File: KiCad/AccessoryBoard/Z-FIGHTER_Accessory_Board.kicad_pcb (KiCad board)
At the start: 2 copper layers, 100 x 75 mm, 24 parts, among them J7 ST7920 Graphic LCD, J9 Conn_02x13_Odd_Even, Q1 BC337, Q2 BC337, SW1 Up (A0), SW2 Down (A1), SW3 Left (A2), SW4 Right (A3), SW5 A (A4), SW6 B (A5)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

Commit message: Updated Accessory Board
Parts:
- J7: footprint Connector_PinSocket_2.54mm:PinSocket_1x20_P2.54mm_Vertical -> Connector_PinSocket_2.54mm:PinSocket_1x20_P2.54mm_Horizontal
- moved J7 6.98 mm to (81.5, 105.6)
- moved Q1 2.44 mm to (81.5, 108.8)
- moved Q2 2.44 mm to (129.8, 108.8)
- moved RB1 2.44 mm to (86.6, 111.3)
- moved RB2 0.44 mm to (138.2, 113.9)
- moved D2 0.10 mm to (145.8, 108.8)
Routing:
- net PB4S: track 80.6 -> 73.6 mm
- net PC0S: track 76.6 -> 69.6 mm
- net PB7S: track 80.6 -> 73.6 mm
- net PB6S: track 80.6 -> 73.6 mm
- net PB5S: track 80.6 -> 73.6 mm
- net PB0S: track 99.2 -> 92.2 mm
- net PB3S: track 77.0 -> 70.0 mm
- net PC2S: track 82.0 -> 75.0 mm
- net PB2S: track 85.2 -> 78.2 mm
- net PC1S: track 79.5 -> 72.6 mm
- net BLK: track 7.72 -> 3.32 mm
- net PB1S: track 87.9 -> 85.0 mm
- net Net-(BZ1-Pad2): track 26.9 -> 25.8 mm
- net Net-(Q2-Pad2): track 10.3 -> 9.50 mm
- net PC3S: track 66.9 -> 66.1 mm
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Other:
- board text added: "Accessory Board Rev. 1c"
- board text removed: "Accessory Board Rev. 1b"

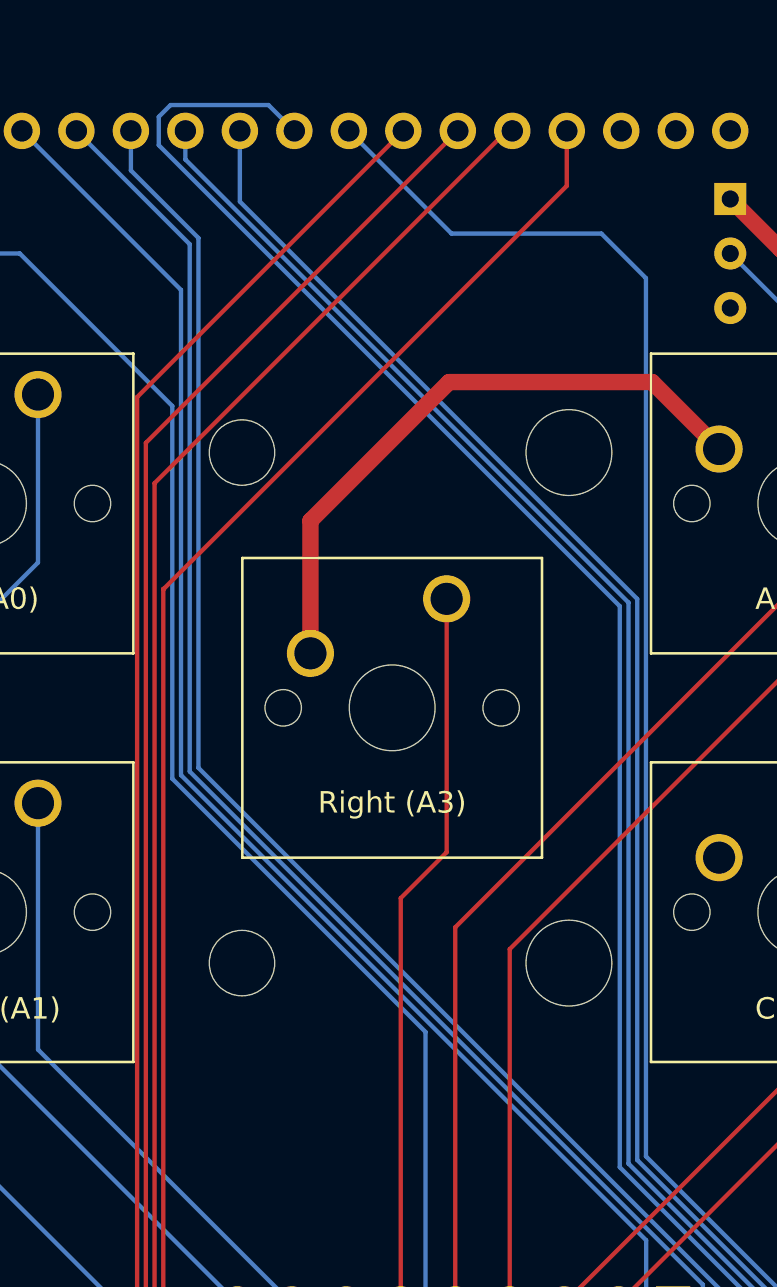
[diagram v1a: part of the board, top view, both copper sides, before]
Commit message: Adjusted routing
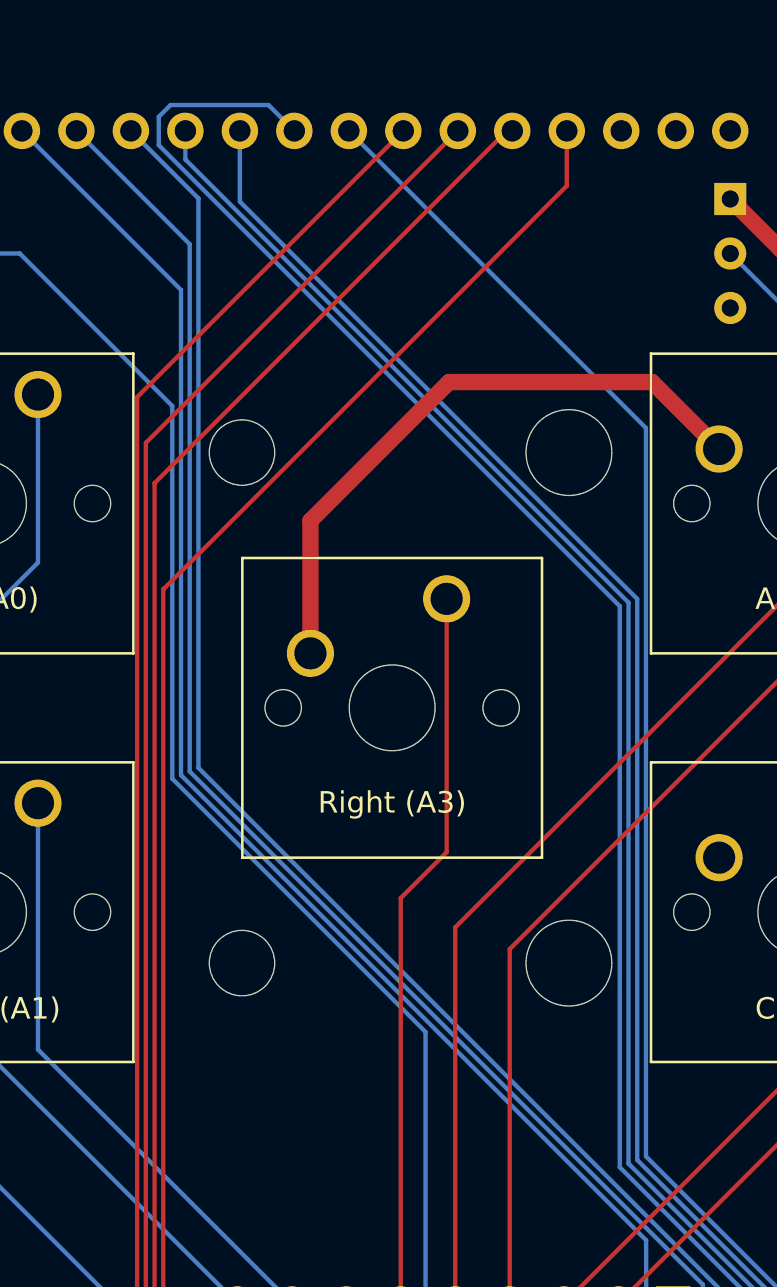
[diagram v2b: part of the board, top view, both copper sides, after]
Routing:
- net PB1S: track 85.0 -> 80.9 mm

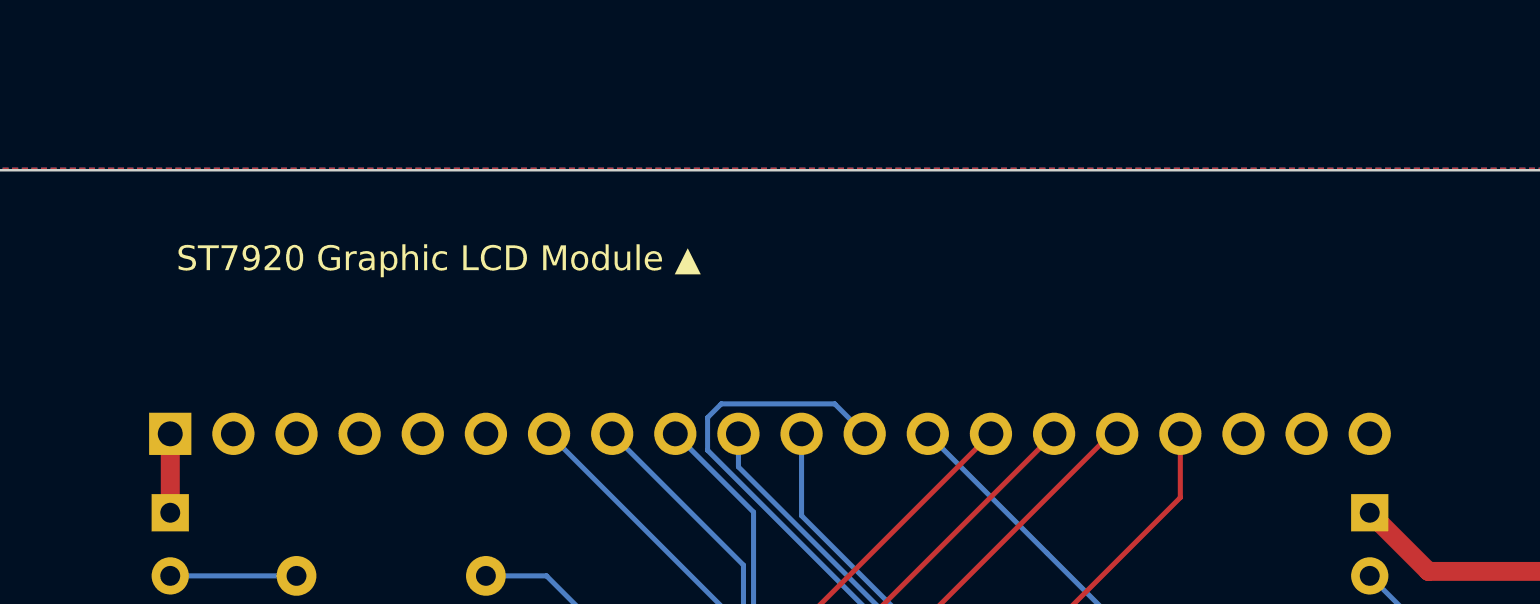
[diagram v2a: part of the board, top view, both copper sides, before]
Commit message: Mainboard improvements
Support for DIP-8 oscillators, replaced system clock pin on CPU control header with CPU #WAIT, added jumper to select internal/external CLOCK2
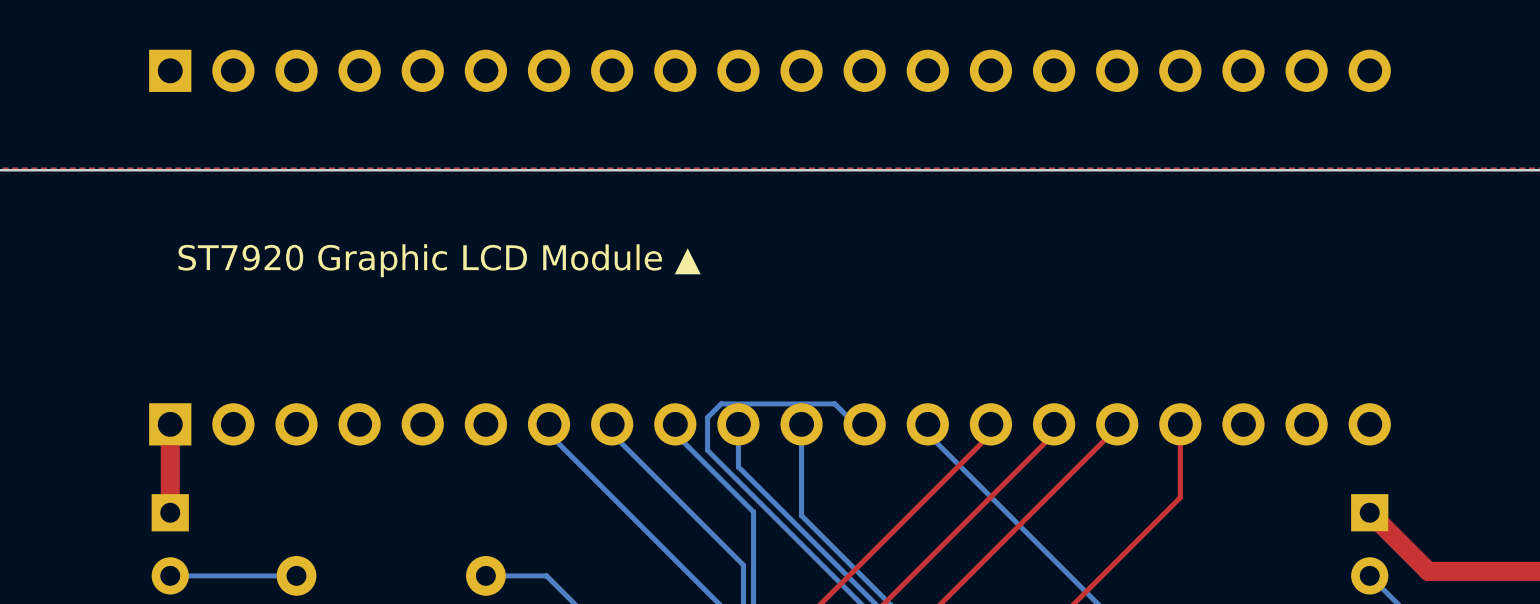
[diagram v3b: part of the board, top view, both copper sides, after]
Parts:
- added J7: ST7920 Graphic LCD, Connector_PinHeader_2.54mm:PinHeader_1x20_P2.54mm_Horizontal, B.Cu at (81.5, 91.0)
- moved J7 0.38 mm to (81.5, 105.2)
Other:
- board text added: "Accessory Board Rev. 1d"
- board text removed: "Accessory Board Rev. 1c"
